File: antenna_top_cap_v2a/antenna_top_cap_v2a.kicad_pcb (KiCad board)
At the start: 4 copper layers, 100 x 100 mm, 74 parts, among them IC1 PCT2075DP,118, J1 Battery Charge Bypass, J10 USB_B_Micro_FC, J11 USB_B_Micro_EPS, J12 FC Board Connector, J13 USB_B_Micro, J14 BM04B-SRSS-TB(LF)(SN), J15 USB_B_Micro, J16 BM04B-SRSS-TB(LF)(SN), J17 BM04B-SRSS-TB(LF)(SN)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

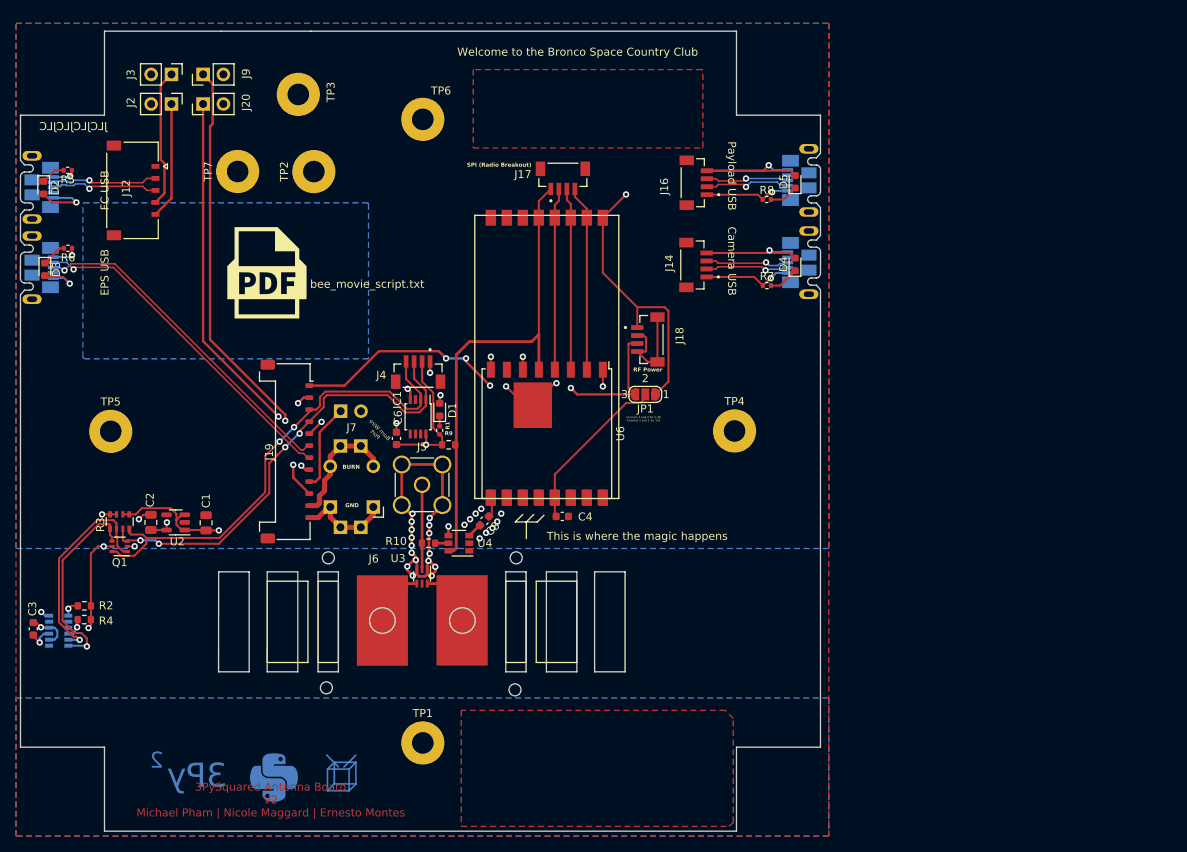
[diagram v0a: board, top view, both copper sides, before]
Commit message: Deleted Unused Parts
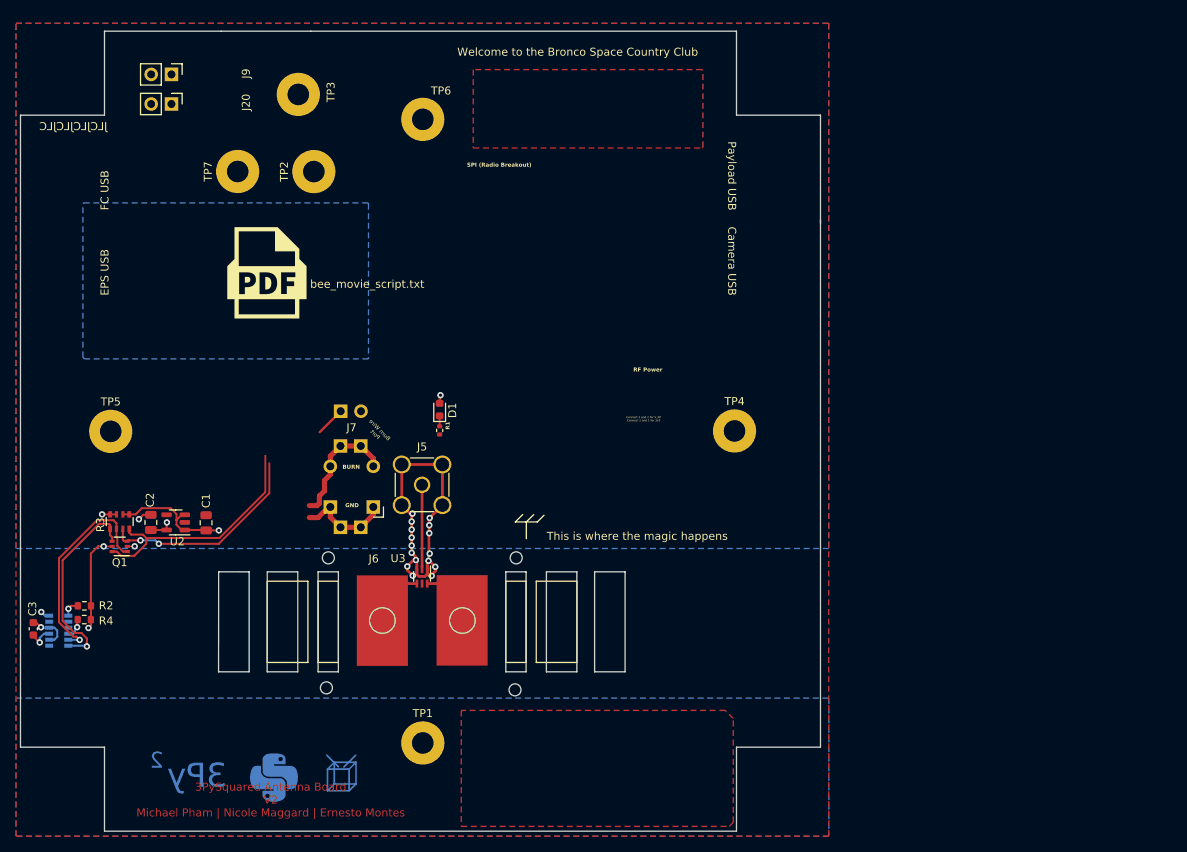
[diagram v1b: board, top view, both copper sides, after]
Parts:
- removed C4: 10uF, Capacitor_SMD:C_0603_1608Metric
- removed C6: 100nf, Capacitor_SMD:C_0603_1608Metric
- removed C8: 100pf, Capacitor_SMD:C_0603_1608Metric
- removed D2, D3, D4, D5: Blue, LED_SMD:LED_0603_1608Metric
- removed IC1: PCT2075DP,118, Package_SO:TSSOP-8_3x3mm_P0.65mm
- removed J10: USB_B_Micro_FC, Antenna_board:MOLEX_105164-0001(round)
- removed J11: USB_B_Micro_EPS, Antenna_board:MOLEX_105164-0001(round)
- removed J12: FC Board Connector, FC_DEV_BOARD:MOLEX_5040500591
- removed J13, J15: USB_B_Micro, Antenna_board:MOLEX_105164-0001(round)
- removed J14, J16, J17, J18, J4: BM04B-SRSS-TB(LF)(SN), Antenna_board:JST_BM04B-SRSS-TB(LF)(SN)
- removed J19: EPS Board Connector, Connector_Molex:Molex_Pico-Lock_504050-1291_1x12-1MP_P1.50mm_Horizontal
- removed J2: EPS USB Bootselect Jumper, Connector_PinHeader_2.54mm:PinHeader_1x02_P2.54mm_Vertical
- removed J3: EPS Reset Jumper, Connector_PinHeader_2.54mm:PinHeader_1x02_P2.54mm_Vertical
- removed JP1: SolderJumper_3_Open, Jumper:SolderJumper-3_P1.3mm_Open_RoundedPad1.0x1.5mm_NumberLabels
- removed R10: DNI, Resistor_SMD:R_0603_1608Metric
- removed R5, R6, R7, R8: 1K, Resistor_SMD:R_0402_1005Metric
- removed R9: 10k, Resistor_SMD:R_0603_1608Metric
- removed REF**: Val**, mainboard:XYZ_cubesat-top
- removed U4: AS193-73LF, Package_TO_SOT_SMD:SuperSOT-6
- removed U5: RFM98PW, Antenna_board:RFM98PW
- removed U6: RFM9xBreakout, Antenna_board:HOPERF_RFM95W_SMD
- R1: value 1K -> 10k
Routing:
- net GND: track 137.7 -> 49.7 mm, vias 41 -> 20
- net SPI0_CS0: track 59.9 -> 0.00 mm
- net +3V3: track 73.4 -> 15.6 mm, vias 6 -> 1
- net ~{EPS_RESET}: track 55.5 -> 0.00 mm, vias 2 -> 0
- net EPS_USBBOOT: track 54.2 -> 0.00 mm, vias 2 -> 0
- net V_RF: track 53.2 -> 0.00 mm, vias 4 -> 0
- net EPS_USB_D+: track 42.3 -> 0.00 mm, vias 1 -> 0
- net EPS_USB_D-: track 42.3 -> 0.00 mm, vias 1 -> 0
- net SDA1: track 57.7 -> 26.4 mm, vias 4 -> 2
- net SCL1: track 61.4 -> 30.5 mm, vias 2 -> 0
- net SPI0_MISO: track 23.2 -> 0.00 mm
- net SPI0_SCK: track 22.8 -> 0.00 mm
- net SPI0_MOSI: track 22.8 -> 0.00 mm
- net RF_VCC: track 21.0 -> 0.00 mm
- net ~{FC_RESET}: track 17.2 -> 0.00 mm
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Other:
- outline, holes or cut-outs redrawn

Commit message: Added USB and DF11 Debug Connector
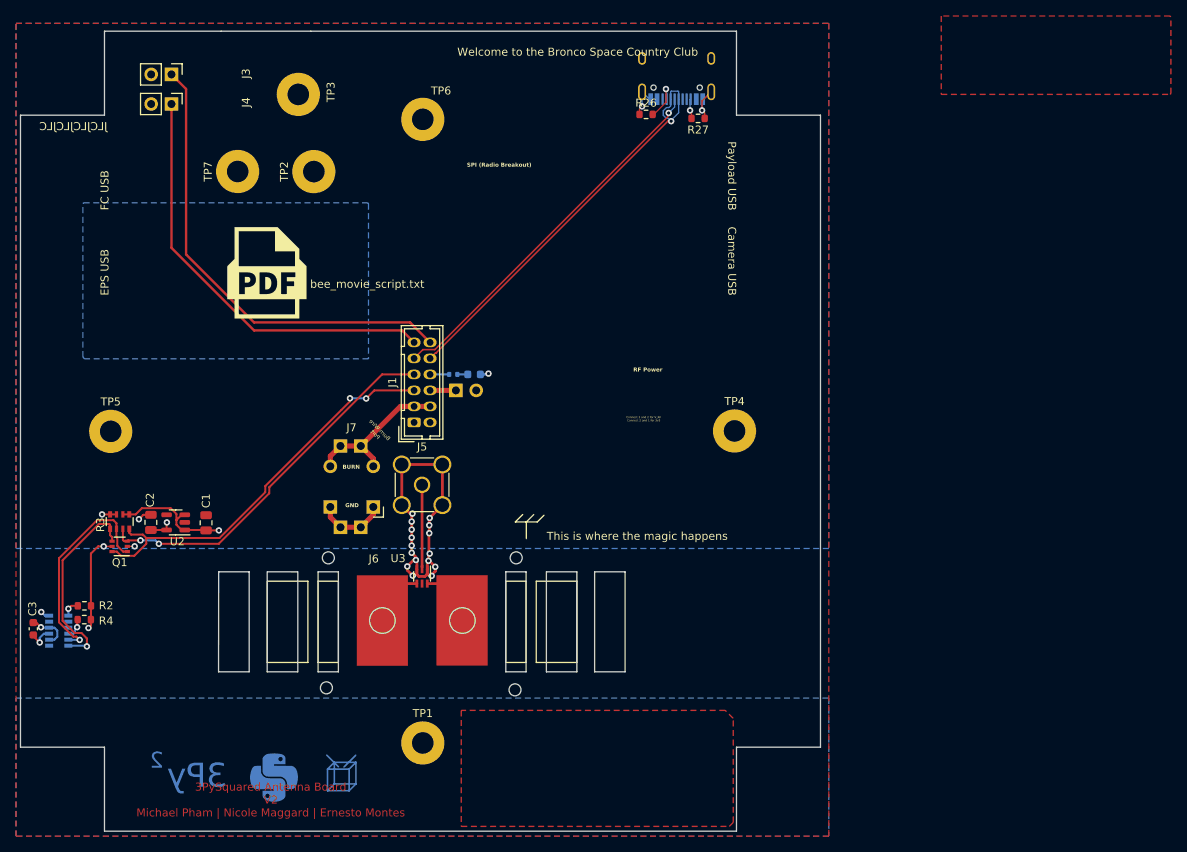
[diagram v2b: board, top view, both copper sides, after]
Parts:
- removed the G*** at (184.7, 74.3)
- added J1: DEBUG, Connector_Hirose:Hirose_DF11-12DP-2DSA_2x06_P2.00mm_Vertical, F.Cu at (164.7, 111.1)
- added J12: USB_C_Receptacle_USB2.0_16P, Connector_USB:USB_C_Receptacle_HRO_TYPE-C-31-M-12, B.Cu at (197.6, 66.7)
- added R26: 5.1k, Resistor_SMD:R_0603_1608Metric, F.Cu at (193.7, 72.6)
- added R27: 5.1k, Resistor_SMD:R_0603_1608Metric, F.Cu at (200.2, 73.1)
- D1, R1: moved to B.Cu
- moved G*** 58.9 mm to (244.6, 63.3)
- moved J2 14.6 mm to (170.0, 107.1)
- moved R1 7.20 mm to (169.6, 105.1), turned to 0 degrees
- moved D1 6.15 mm to (172.2, 105.1), turned to 0 degrees
- renumbered J1 to J2, J9 to J3, J20 to J4
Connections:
- net SCL1 renamed SCL0
- net SDA1 renamed SDA0
- J7 pad 2: BURN_GND -> GND
- TP1 pad 1: GND -> unconnected-(TP1-Pad1)
- TP2 pad 1: GND -> unconnected-(TP2-Pad1)
- TP3 pad 1: GND -> unconnected-(TP3-Pad1)
- TP4 pad 1: GND -> unconnected-(TP4-Pad1)
- TP5 pad 1: GND -> unconnected-(TP5-Pad1)
- TP6 pad 1: GND -> unconnected-(TP6-Pad1)
- TP7 pad 1: GND -> unconnected-(TP7-Pad1)
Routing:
- net ~{FC_RESET}: track 0.00 -> 58.3 mm
- net FC_USBBOOT: track 0.00 -> 53.2 mm
- net USB_D-: track 0.00 -> 52.4 mm, vias 0 -> 1
- net USB_D+: track 0.00 -> 46.8 mm, vias 0 -> 1
- net SDA0: track 26.4 -> 47.3 mm
- net GND: track 49.7 -> 70.1 mm, vias 20 -> 22
- net SCL0: track 30.5 -> 50.5 mm, vias 0 -> 2
- net BURN_GND: track 12.2 -> 0.00 mm
- net Net-(J12-CC1): track 0.00 -> 5.25 mm, vias 0 -> 1
- net BURN: track 15.9 -> 20.1 mm
- net Net-(J12-CC2): track 0.00 -> 2.51 mm, vias 0 -> 1
- net +3V3: track 15.6 -> 18.0 mm
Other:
- outline, holes or cut-outs redrawn
- board text added: "NOT TODAY PROTON! THE POWER OF FAULT TOLERANCE COMPELS YOU"
- board text removed: "EPS Jumpers"
- board text removed: "Henry Fung | Shreya Kolla | Kaitlyn Tseng Krishiv Aggarwal | Arush Khare | Natalie Zheng Raza Pathan | Diya Dalal | Shreeansh Rathi Shruti Senthilram | Venkata Donthireddy | Eric Bao Patrick Ren | Jerry Sun | Matthew Chan | Mason Kuan Chinmayee Walavalkar | William Yang | Arjun Vivek"
- board text removed: "Irvington High School Girls in STEM Club"
- board text removed: "NOT TODAY PROTON! THE POWER OF MRAM COMPELS YOU"
- board text removed: "Pleiades Orpheus Leads the Way!"

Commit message: Added MCP Temperature Sensor
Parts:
- added C43: 1uF, Capacitor_SMD:C_0805_2012Metric, F.Cu at (147.7, 106.6)
- added U16: MCP9808T-E/MS, Package_SO:MSOP-8-1EP_3x3mm_P0.65mm_EP1.5x1.8mm_ThermalVias, F.Cu at (152.3, 107.0)
- moved G*** 51.8 mm to (188.7, 95.1)
- moved J2 48.0 mm to (140.2, 69.5)
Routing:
- net Dir_Chrg_In: track 3.23 -> 65.6 mm, vias 0 -> 2
- net GND: track 70.1 -> 78.5 mm, vias 22 -> 24
- net SDA0: track 47.3 -> 53.5 mm, vias 2 -> 4
- net +3V3: track 18.0 -> 23.7 mm, vias 1 -> 2
- net SCL0: track 50.5 -> 53.2 mm
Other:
- board text added: "The PROVES Kit V3"
- board text removed: "The PROVES Kit V1.5"
